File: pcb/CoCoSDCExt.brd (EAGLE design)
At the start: 101.6 x 47 mm, 48 parts, among them IC1 AM29F040J, IC10 YAC512-M, IC14 TL974, IC15 TL974, IC2 XC9572XLVQG64, IC9 YMF262-M, X1 EXPANSION_PORT_COCO, X2 EXPANSION_PORT_COCOS

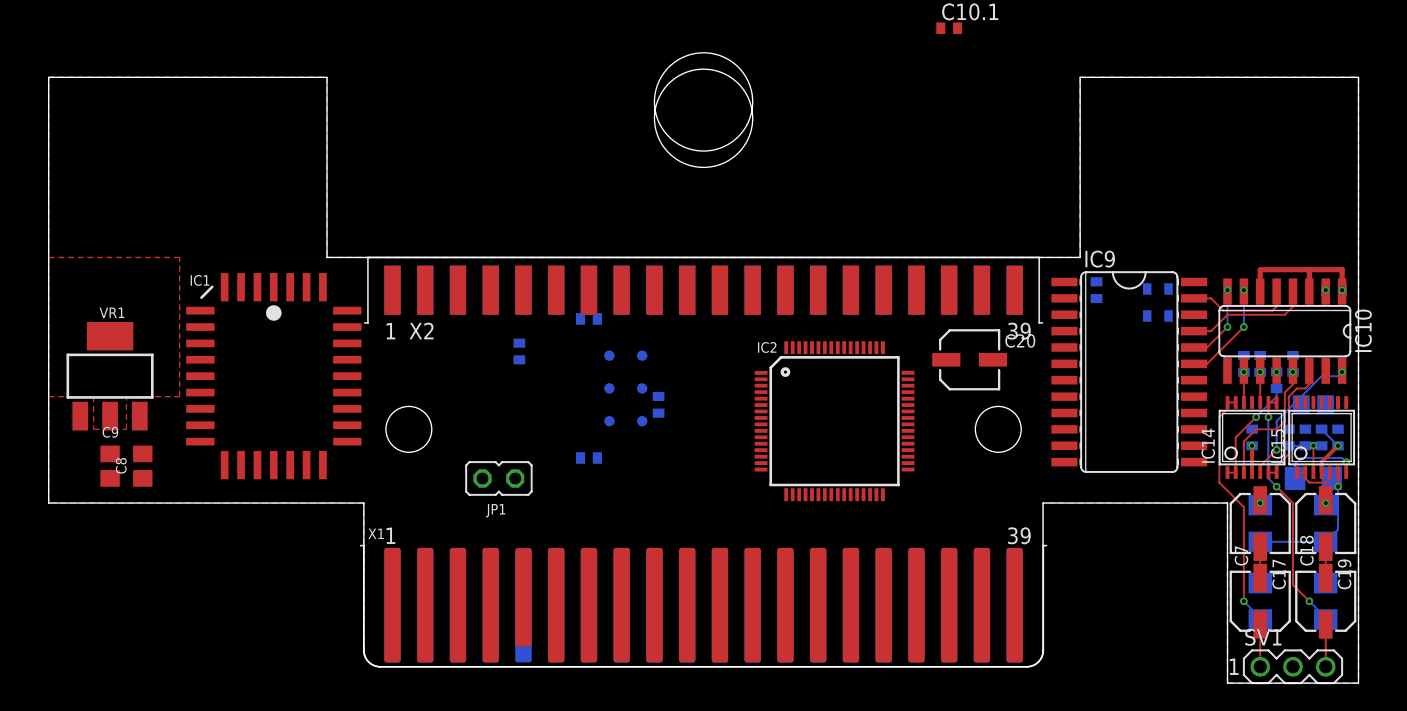
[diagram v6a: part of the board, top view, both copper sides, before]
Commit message: routing pass-thru connector
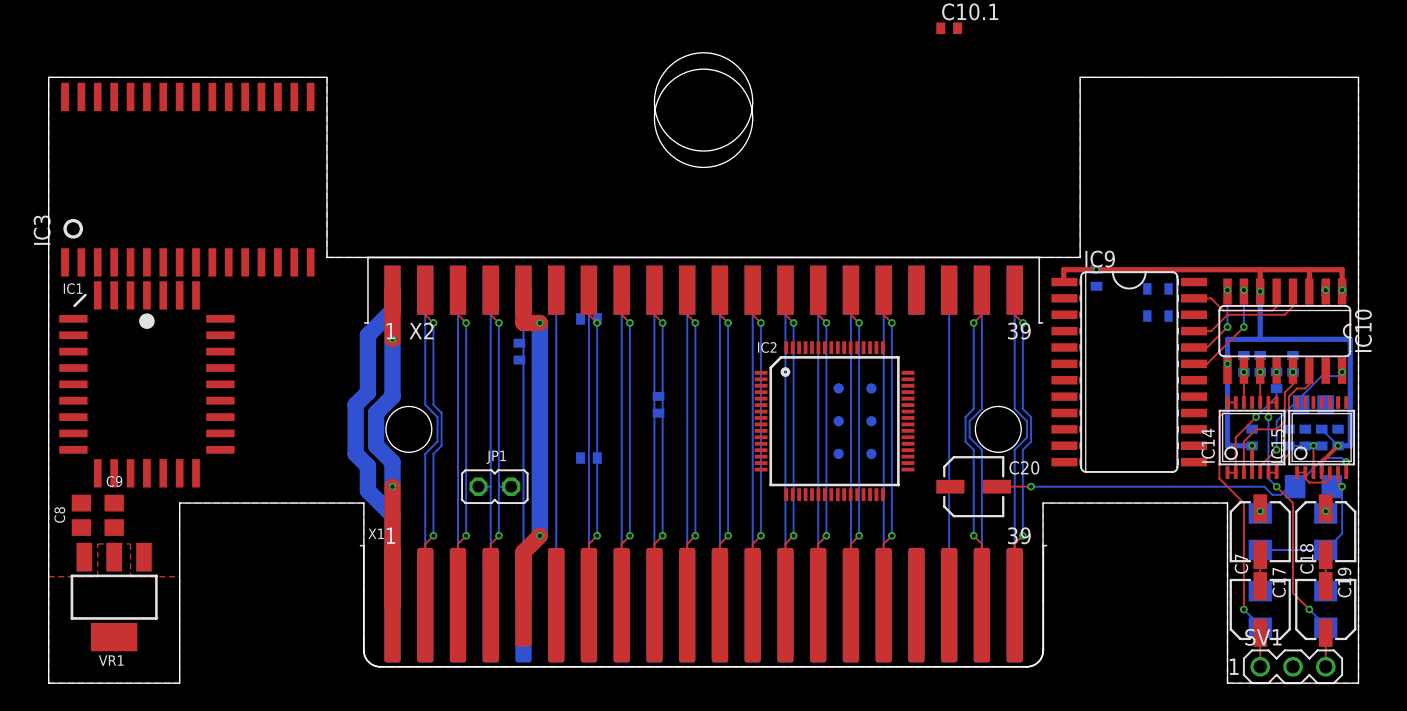
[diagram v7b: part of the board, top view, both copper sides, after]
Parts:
- added IC3: AS6C4008SIN, memory-alliance:SOP32L
- moved 3V3 18.0 mm to (10.5, 21.6)
- moved GND 18.0 mm to (13.0, 19.1)
- moved TCK 18.0 mm to (13.0, 16.5)
- moved TDI 18.0 mm to (10.5, 16.5)
- moved TDO 18.0 mm to (13.0, 21.6)
- moved TMS 18.0 mm to (10.5, 19.1)
- moved VR1 17.1 mm to (-45.7, 5.40), turned to 180 degrees
- moved IC1 9.86 mm to (-43.2, 21.9)
- moved C20 9.85 mm to (21.0, 14.0)
- moved C8 6.10 mm to (-48.3, 11.7)
- moved C9 3.82 mm to (-45.7, 11.7)
- moved C9.1 0.95 mm to (30.5, 30.2)
- moved JP1 0.71 mm to (-16.2, 14.0), turned to 90 degrees
- moved C17 0.64 mm to (43.2, 10.5)
- moved C19 0.64 mm to (48.3, 10.5)
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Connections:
- new net !HALT: X1.3, X2.3
- new net !NMI: X1.4, X2.4
- net +5V: now also X2.9
- net GND: now also IC3.16
- net VCC: now also IC3.32; no longer X2.9
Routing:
- net +5V: track 18.0 -> 92.9 mm, vias 3 -> 8
- net +12V: track 0.00 -> 26.8 mm
- net Q: track 0.00 -> 25.9 mm, vias 0 -> 2
- net A15: track 0.00 -> 25.5 mm, vias 0 -> 2
- net A13: track 0.00 -> 25.5 mm, vias 0 -> 2
- net -12V: track 0.00 -> 25.5 mm, vias 0 -> 2
- net !HALT: track 0.00 -> 25.5 mm, vias 0 -> 2
- net A10: track 0.00 -> 25.4 mm, vias 0 -> 2
- net !CART: track 0.00 -> 25.4 mm
- net A14: track 0.00 -> 25.2 mm
- net !SLENB: track 0.00 -> 25.2 mm
- net !NMI: track 0.00 -> 25.2 mm
- net D7: track 0.00 -> 25.0 mm, vias 0 -> 2
- net D5: track 0.00 -> 25.0 mm, vias 0 -> 2
- net D3: track 0.00 -> 25.0 mm, vias 0 -> 2
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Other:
- outline, holes or cut-outs redrawn

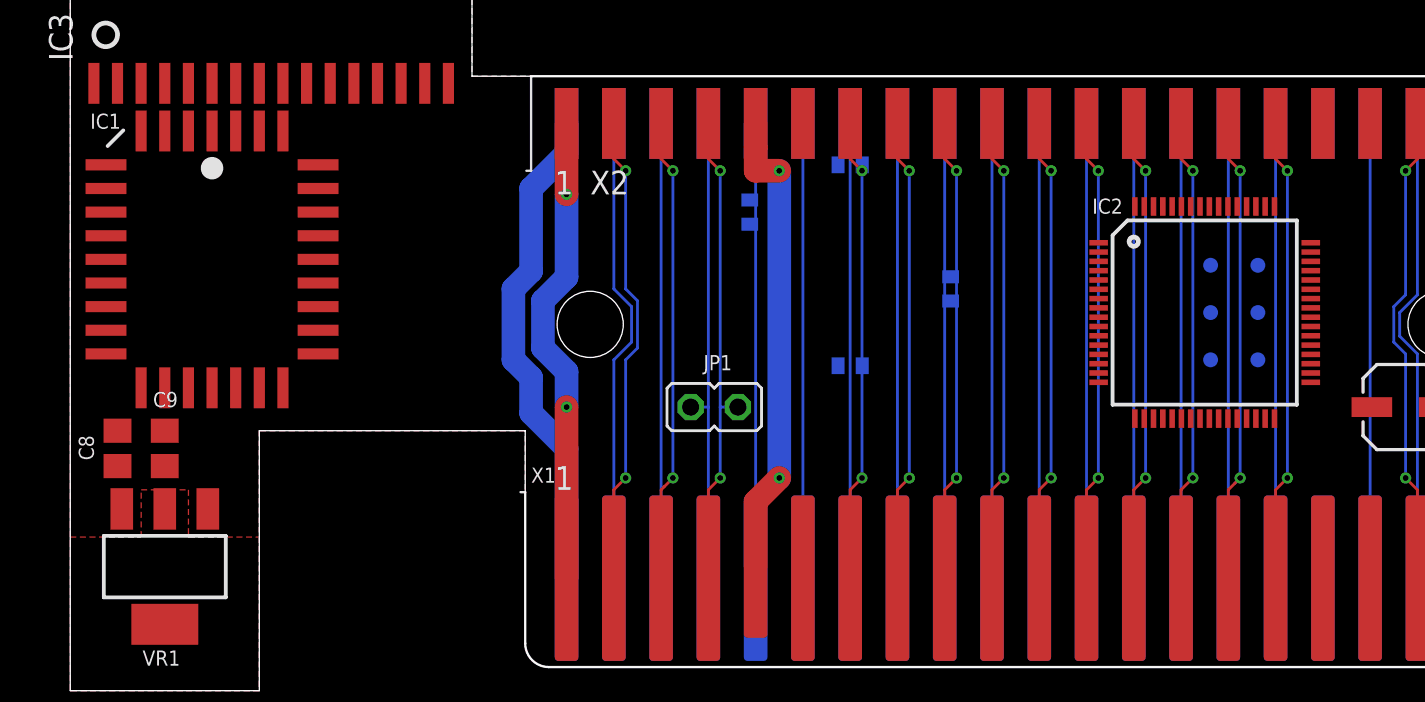
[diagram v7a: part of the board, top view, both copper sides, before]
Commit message: Routing address lines for flash/ram
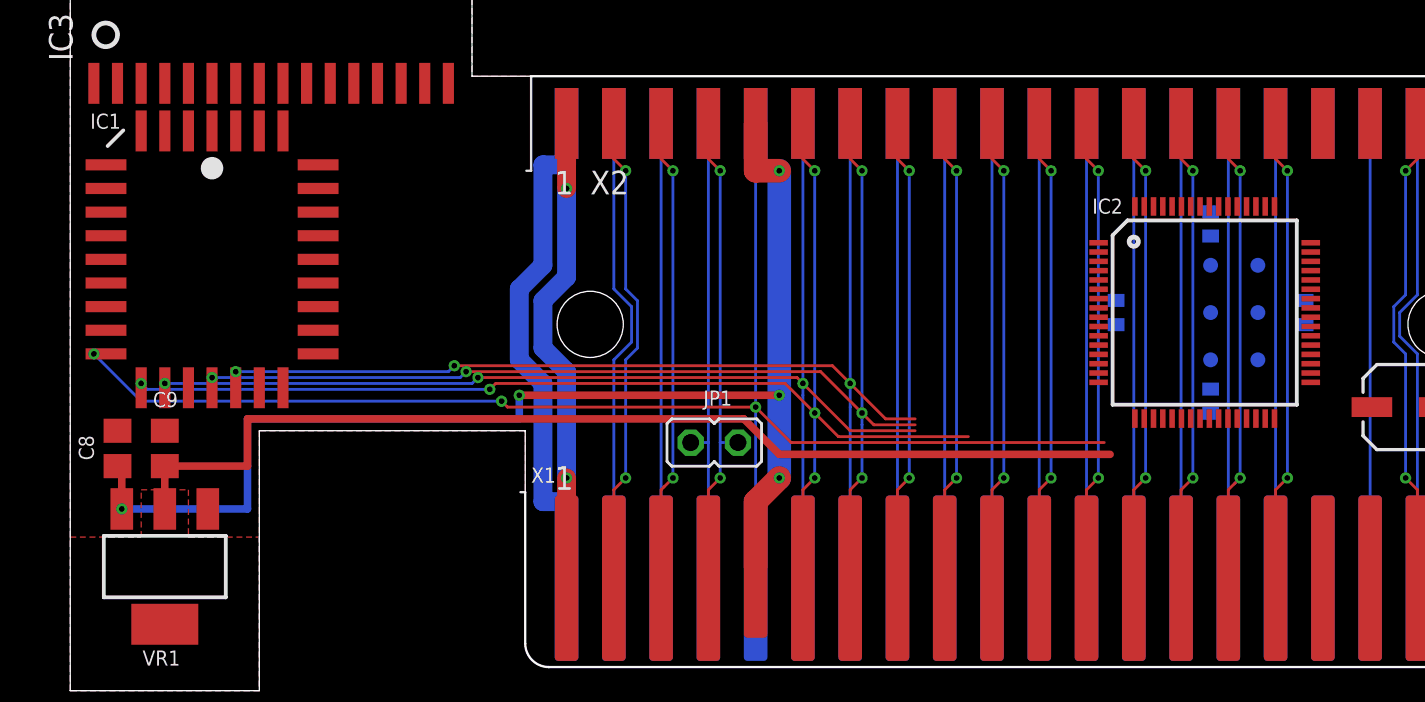
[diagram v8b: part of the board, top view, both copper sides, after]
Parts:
- moved C2.2 20.4 mm to (5.40, 19.1)
- moved C2.1 19.6 mm to (10.5, 23.8), turned to 270 degrees
- moved C2.3 19.5 mm to (10.5, 14.3), turned to 90 degrees
- moved C2.4 19.1 mm to (15.6, 19.1)
- moved JP1 1.91 mm to (-16.2, 12.1)
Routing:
- net D1: track 0.00 -> 71.1 mm, vias 0 -> 5
- net D0: track 24.4 -> 81.3 mm, vias 0 -> 3
- net +3V3: track 0.00 -> 56.4 mm
- net +5V: track 92.9 -> 137.8 mm, vias 8 -> 11
- net D2: track 24.4 -> 66.3 mm, vias 0 -> 3
- net D3: track 25.0 -> 64.6 mm, vias 2 -> 5
- net D4: track 24.4 -> 63.1 mm, vias 0 -> 3
- net +12V: track 26.8 -> 28.0 mm
